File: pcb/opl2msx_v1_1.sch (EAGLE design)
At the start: 26 parts, among them IC1 74HC32N, IC2 74HC138N, IC3 YM3812, IC4 Y3014B, IC5 LM358N, IC6 7404N, IC7 LM386N-1, IC8 29EE010N, J1 AUDIO_JACK_3.5MM_KIT

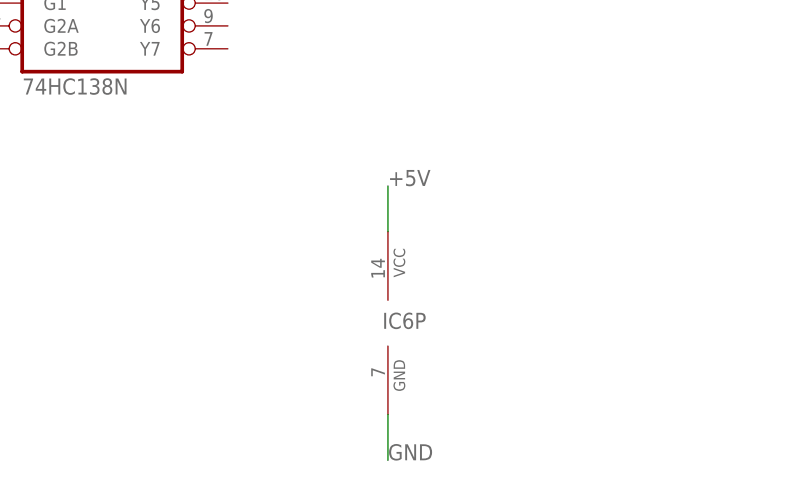
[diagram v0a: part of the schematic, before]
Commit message: Fixed PCB version 1.1. Removed unused 7404 IC
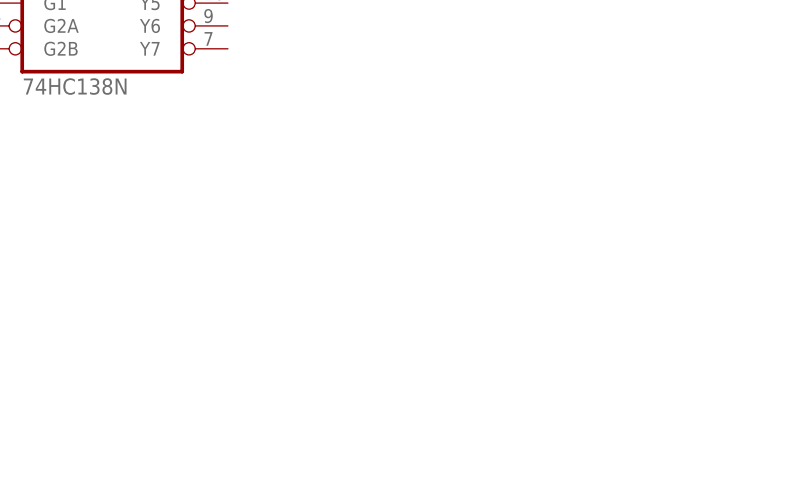
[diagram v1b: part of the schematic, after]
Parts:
- removed IC6: 7404N, 74xx-us:7404N
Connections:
- net +5V: no longer IC6P.VCC
- net GND: no longer IC6P.GND
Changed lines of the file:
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@@
 <part name="C1" library="rcl" deviceset="C-EU" device="050-024X044" value="100nF"/>
 <part name="IC5" library="linear" deviceset="LM358" device="N"/>
-<part name="IC6" library="74xx-us" deviceset="74*04" device="N"/>
 <part name="IC7" library="linear" deviceset="LM386?-*" device="N" technology="1"/>
 <part name="C2" library="rcl" deviceset="CPOL-US" device="E2.5-6" value="10uF"/>
@@
 <instance part="C3" gate="G$1" x="55.118" y="20.32" rot="R180"/>
 <instance part="IC5" gate="P" x="-17.78" y="12.7"/>
-<instance part="IC6" gate="P" x="127" y="15.24"/>
 <instance part="C7" gate="G$1" x="277.368" y="218.44" rot="R180"/>
 <instance part="R5" gate="G$1" x="277.368" y="208.788" rot="R90"/>
@@
 </segment>
 <segment>
-<pinref part="IC6" gate="P" pin="GND"/>
-<wire x1="127" y1="5.08" x2="127" y2="0" width="0.1524" layer="91"/>
-<label x="127" y="0" size="1.778" layer="95"/>
-</segment>
-<segment>
 <pinref part="R5" gate="G$1" pin="1"/>
 <wire x1="277.368" y1="195.58" x2="281.94" y2="195.58" width="0.1524" layer="91"/>
@@
 </segment>
 <segment>
-<pinref part="IC6" gate="P" pin="VCC"/>
-<wire x1="127" y1="25.4" x2="127" y2="30.48" width="0.1524" layer="91"/>
-<label x="127" y="30.48" size="1.778" layer="95"/>
-</segment>
-<segment>
